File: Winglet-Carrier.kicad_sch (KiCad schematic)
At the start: 8 parts, among them M1 Mount_M3, M2 Mount_M3, M3 Mount_M3, M4 Mount_M3

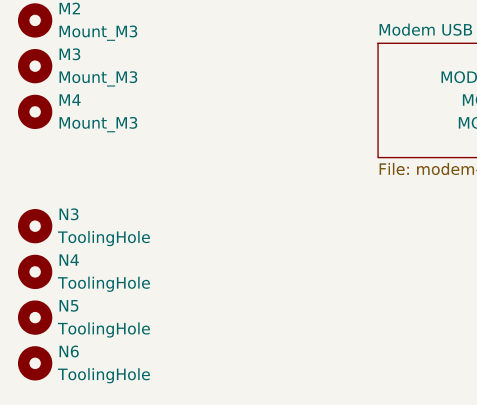
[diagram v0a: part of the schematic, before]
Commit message: Reannotate components
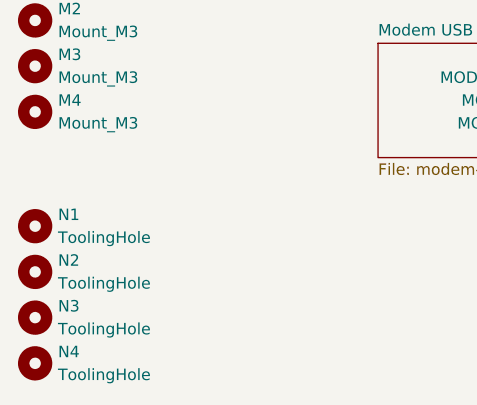
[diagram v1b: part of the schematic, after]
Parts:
- renumbered N3 to N1, N4 to N2, N5 to N3, N6 to N4
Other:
- company: (none) -> TL Embedded
- title: (none) -> Winglet Carrier Board
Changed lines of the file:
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@@
 	(generator_version "8.0")
 	(paper "A4")
+	(title_block
+		(title "Winglet Carrier Board")
+		(date "2024-08-09")
+		(rev "v1.0")
+		(company "TL Embedded")
+	)
 	(wire
 		(pts
@@
 		(dnp no)
 		(fields_autoplaced yes)
-		(property "Reference" "N5"
+		(property "Reference" "N3"
 			(at 40.64 110.4899 0)
 			(effects
@@
 			(project "Winglet-Carrier"
 				(path "/bbb905ef-a222-43ea-83e2-d1132f7d94bb"
-					(reference "N5")
+					(reference "N3")
 					(unit 1)
 				)
@@
 		(dnp no)
 		(fields_autoplaced yes)
-		(property "Reference" "N4"
+		(property "Reference" "N2"
 			(at 40.64 105.4099 0)
 			(effects
@@
 			(project "Winglet-Carrier"
 				(path "/bbb905ef-a222-43ea-83e2-d1132f7d94bb"
-					(reference "N4")
+					(reference "N2")
 					(unit 1)
 				)
@@
 		(dnp no)
 		(fields_autoplaced yes)
-		(property "Reference" "N6"
+		(property "Reference" "N4"
 			(at 40.64 115.5699 0)
 			(effects
@@
 			(project "Winglet-Carrier"
 				(path "/bbb905ef-a222-43ea-83e2-d1132f7d94bb"
-					(reference "N6")
+					(reference "N4")
 					(unit 1)
 				)
@@
 		(on_board yes)
 		(dnp no)
-		(property "Reference" "N3"
+		(property "Reference" "N1"
 			(at 40.64 100.3299 0)
 			(effects
@@
 			(project ""
 				(path "/bbb905ef-a222-43ea-83e2-d1132f7d94bb"
-					(reference "N3")
+					(reference "N1")
 					(unit 1)
 				)
